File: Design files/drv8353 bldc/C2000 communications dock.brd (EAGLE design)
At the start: 160 x 100 mm, 3 parts, among them IC1 ADUM1311ARWZ, J3 SS-6488-NF-A431

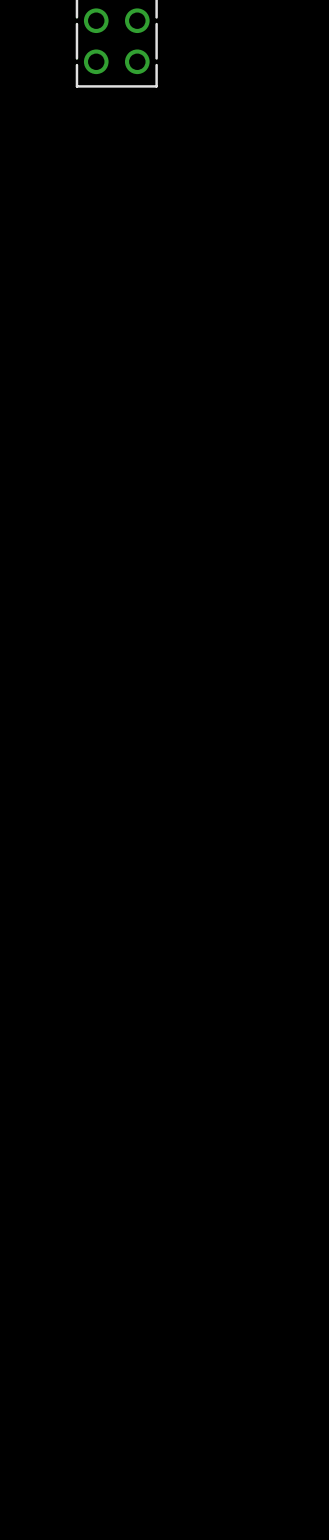
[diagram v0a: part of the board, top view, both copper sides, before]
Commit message: did some wiring and added led's
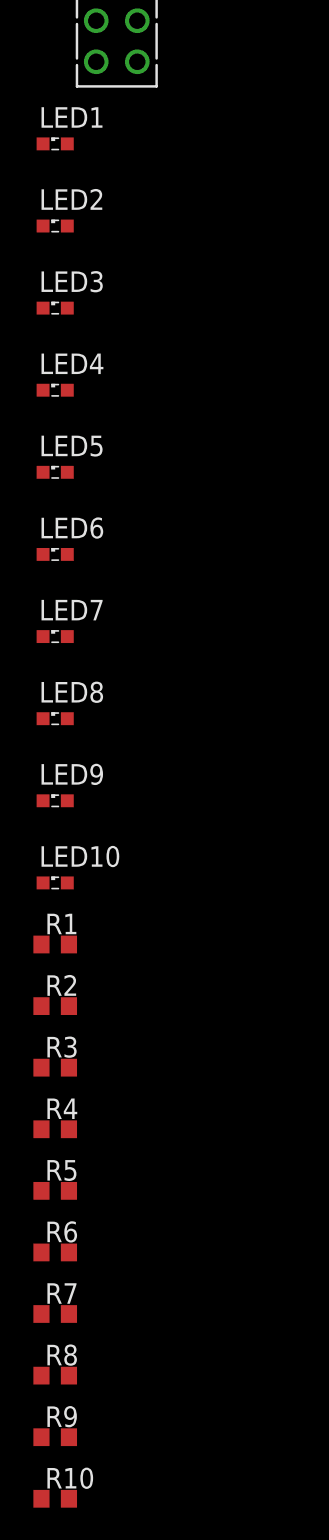
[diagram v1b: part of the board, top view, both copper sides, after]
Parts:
- added LED1, LED10, LED2, LED3, LED4, LED5, LED6, LED7, LED8, LED9: (no value), eagle-ltspice:LED_SML0603
- added R1, R10, R2, R3, R4, R5, R6, R7, R8, R9: 50, rcl:R0603
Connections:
- removed net 5V: U$1.21
- new net N$1: IC1.3, J3.3
- new net N$10: IC1.1, J3.1
- new net N$11: LED8.A, U$1.33
- new net N$12: LED9.A, U$1.32
- new net N$13: IC1.4, J3.4
- new net N$14: IC1.5, J3.5
- new net N$15: LED10.A, U$1.31
- new net N$16: IC1.2, IC1.7, IC1.8, J3.2
- new net N$17: LED1.C, R1.2
- new net N$18: LED2.C, R2.2
- new net N$19: LED3.C, R3.2
- new net N$2: LED1.A, U$1.40
- new net N$20: LED4.C, R4.2
- new net N$21: LED5.C, R5.2
- new net N$22: LED6.C, R6.2
- new net N$23: LED7.C, R7.2
- new net N$24: LED8.C, R8.2
- new net N$25: LED9.C, R9.2
- new net N$26: LED10.C, R10.2
- new net N$3: LED2.A, U$1.39
- new net N$4: LED3.A, U$1.38
- new net N$5: LED4.A, U$1.37
- new net N$6: LED5.A, U$1.36
- new net N$8: LED6.A, U$1.35
- new net N$9: LED7.A, U$1.34
- net 3.3V: now also IC1.16
- net CLK: now also IC1.13
- net GND: now also IC1.10, IC1.15, IC1.9, R1.1, R10.1, R2.1, R3.1, R4.1, R5.1, R6.1, R7.1, R8.1, R9.1, U$1.18
- net MISO: now also IC1.12
- net MOSI: now also IC1.14

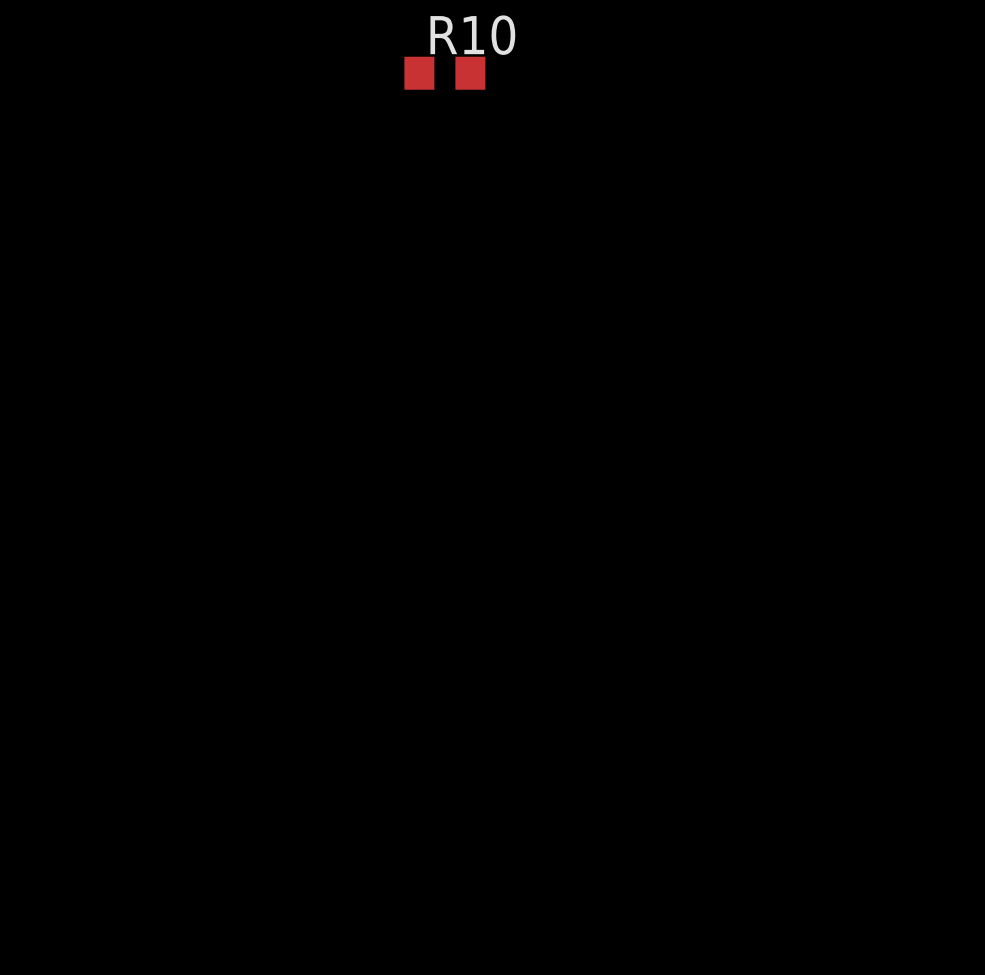
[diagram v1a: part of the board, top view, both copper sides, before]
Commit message: added pot, and headers for spi , i2c, analog pins, and the input spi signal
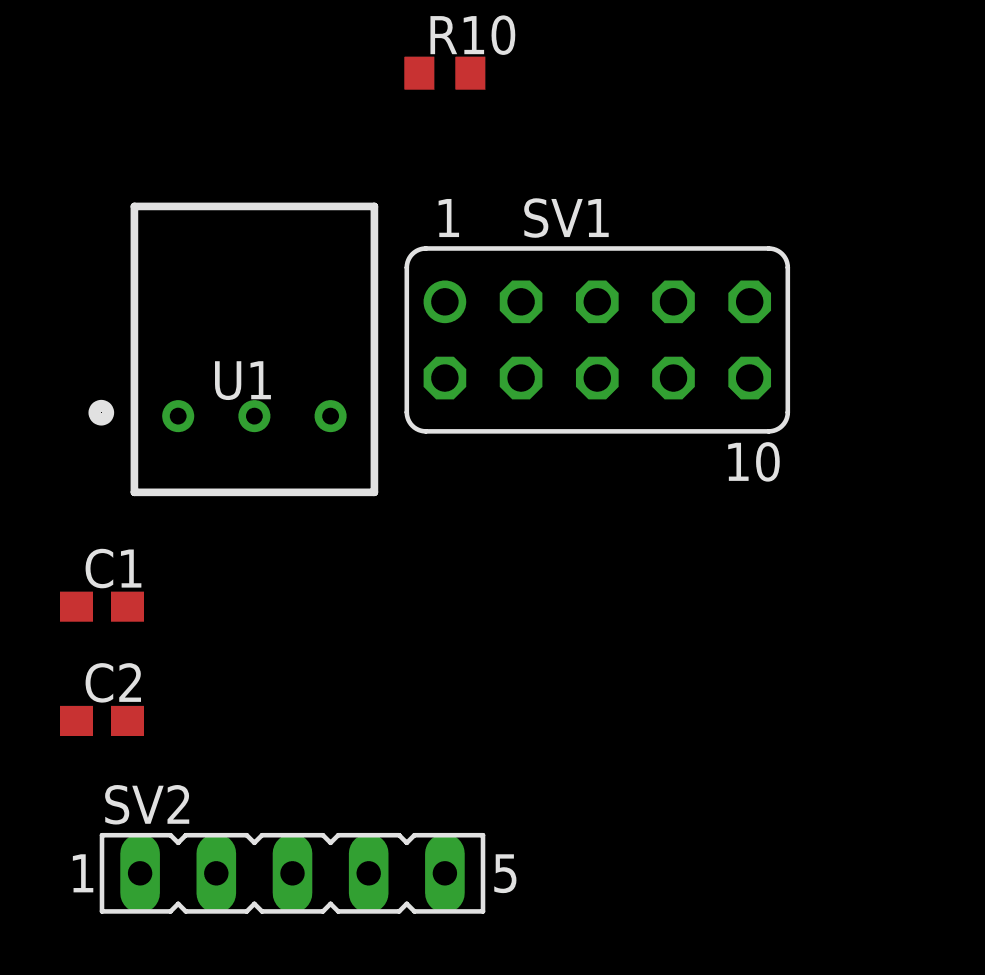
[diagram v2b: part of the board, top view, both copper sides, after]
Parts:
- added C1, C2: (no value), rcl:C0603
- added SV1: (no value), con-lsta:FE05-2
- added SV2: (no value), con-lsta:FE05-1
- added U1: 3352T-1-203LF, SamacSys_Parts:3352T-1-203LF
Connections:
- new net 5V: SV1.9, U$1.21
- new net AI1: SV1.8, U$1.23
- new net AI2: SV1.6, U$1.24
- new net POT: U$1.25, U1.2
- new net SCL: SV1.2, U$1.9
- new net SDA: SV1.4, U$1.10
- net 3.3V: now also C2.1, SV1.7, U1.3
- net CLK: now also SV1.5
- net GND: now also C2.2, SV1.10, U1.1; no longer U$1.18
- net MISO: now also SV1.1
- net MOSI: now also SV1.3
- net N$1: now also SV2.3
- net N$10: now also C1.1, SV2.1
- net N$13: now also SV2.4
- net N$14: now also SV2.5
- net N$16: now also C1.2, SV2.2

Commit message: reordered header and did a tenative layout
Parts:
- moved SV2 223.0 mm to (27.9, 40.6), turned to 180 degrees
- moved C1 213.3 mm to (29.3, 37.5), turned to 180 degrees
- moved C2 203.6 mm to (29.5, 23.5), turned to 180 degrees
- moved SV1 174.8 mm to (30.5, 10.7), turned to 270 degrees
- moved U1 174.0 mm to (17.8, 7.62), turned to 180 degrees
- moved R10 165.6 mm to (40.6, 5.08)
- moved R9 164.4 mm to (40.6, 7.62)
- moved R8 163.2 mm to (40.6, 10.2)
- moved R7 162.0 mm to (40.6, 12.7)
- moved R6 160.8 mm to (40.6, 15.2)
- moved R5 159.7 mm to (40.6, 17.8)
- moved R4 158.5 mm to (40.6, 20.3)
- moved R3 157.3 mm to (40.6, 22.9)
- moved R2 156.1 mm to (40.6, 25.4)
- moved R1 154.9 mm to (40.6, 27.9)
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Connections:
- net N$1 renamed EMOSI
- net N$10 renamed EVD
- net N$13 renamed ECLK
- net N$14 renamed EMISO
- net N$16 renamed EGND
- net 3.3V: now also SV1.1; no longer SV1.7
- net 5V: now also SV1.2; no longer SV1.9
- net AI1: now also SV1.4; no longer SV1.8
- net CLK: now also SV1.8; no longer SV1.5
- net GND: now also SV1.7; no longer SV1.10
- net MISO: now also SV1.5; no longer SV1.1
- net POT: now also U$1.28; no longer U$1.25
- net SCL: now also SV1.10; no longer SV1.2
- net SDA: now also SV1.9; no longer SV1.4
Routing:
- net 3.3V: track 0.00 -> 70.1 mm
- net CLK: track 0.00 -> 41.0 mm, vias 0 -> 2
- net MISO: track 0.00 -> 37.9 mm
- net GND: track 0.00 -> 37.5 mm, vias 0 -> 20
- net MOSI: track 0.00 -> 37.4 mm, vias 0 -> 2
- net SDA: track 0.00 -> 28.1 mm
- net 5V: track 0.00 -> 26.6 mm
- net EVD: track 0.00 -> 26.1 mm
- net AI2: track 0.00 -> 25.6 mm
- net AI1: track 0.00 -> 25.6 mm
- net SCL: track 0.00 -> 25.4 mm
- net EGND: track 0.00 -> 20.6 mm, vias 0 -> 2
- net EMOSI: track 0.00 -> 20.3 mm
- net EMISO: track 0.00 -> 13.8 mm
- net ECLK: track 0.00 -> 13.3 mm
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- added copper zone on layer 16, net EGND
- added copper zone on layer 16, net GND
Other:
- board size 160 x 100 mm -> 55.9 x 53 mm

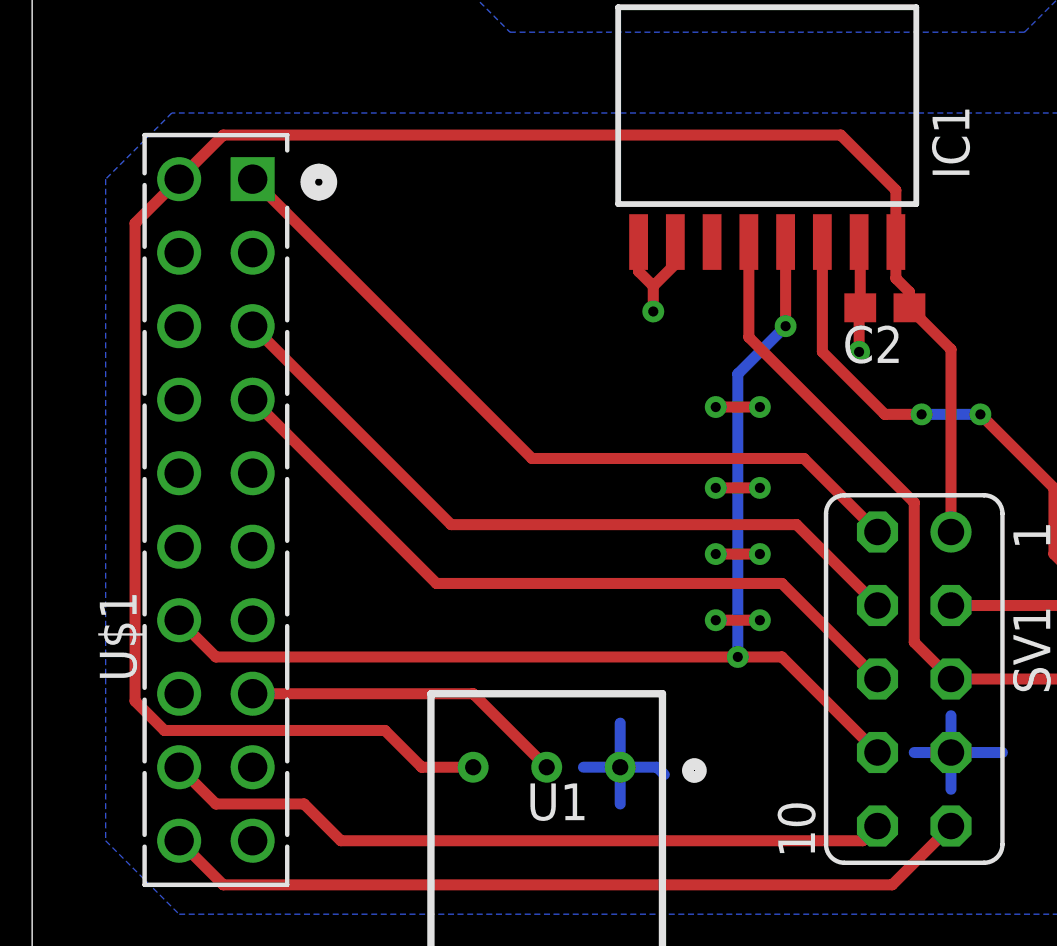
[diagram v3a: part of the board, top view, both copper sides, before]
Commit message: moved analog signals top adc-b pins
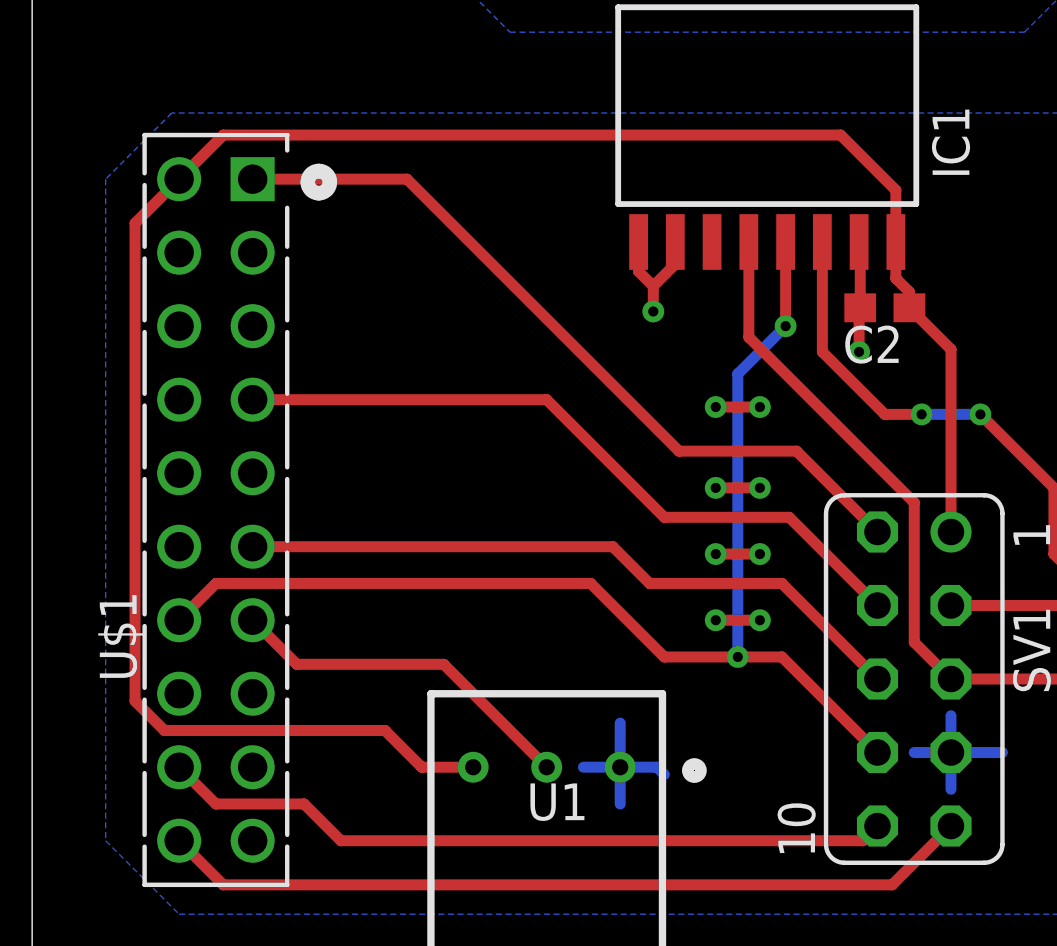
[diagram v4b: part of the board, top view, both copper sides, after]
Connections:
- net AI1: now also U$1.24; no longer U$1.23
- net AI2: now also U$1.26; no longer U$1.24
- net POT: now also U$1.27; no longer U$1.28
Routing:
- net AI2: track 25.6 -> 23.5 mm
- net AI1: track 25.6 -> 24.5 mm
- net POT: track 11.2 -> 12.3 mm
- net CLK: track 41.0 -> 42.1 mm
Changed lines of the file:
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@@
 <contactref element="SV1" pad="8"/>
 <wire x1="29.21" y1="8.128" x2="25.908" y2="11.43" width="0.381" layer="1"/>
-<wire x1="6.35" y1="11.43" x2="5.08" y2="12.7" width="0.381" layer="1"/>
 <wire x1="25.908" y1="11.43" x2="24.384" y2="11.43" width="0.381" layer="1"/>
-<wire x1="24.384" y1="11.43" x2="6.35" y2="11.43" width="0.381" layer="1"/>
 <via x="24.384" y="11.43" extent="1-16" drill="0.35"/>
 <via x="26.035" y="22.86" extent="1-16" drill="0.35"/>
@@
 <wire x1="24.384" y1="21.209" x2="26.035" y2="22.86" width="0.381" layer="16"/>
 <wire x1="26.035" y1="22.86" x2="26.035" y2="25.768" width="0.381" layer="1"/>
+<wire x1="24.384" y1="11.43" x2="21.844" y2="11.43" width="0.381" layer="1"/>
+<wire x1="19.304" y1="13.97" x2="6.35" y2="13.97" width="0.381" layer="1"/>
+<wire x1="6.35" y1="13.97" x2="5.08" y2="12.7" width="0.381" layer="1"/>
+<wire x1="21.844" y1="11.43" x2="19.304" y2="13.97" width="0.381" layer="1"/>
 </signal>
 <signal name="EVD">
@@
 <contactref element="U$1" pad="21"/>
 <contactref element="SV1" pad="2"/>
-<wire x1="29.21" y1="15.748" x2="26.67" y2="18.288" width="0.381" layer="1"/>
-<wire x1="17.272" y1="18.288" x2="7.62" y2="27.94" width="0.381" layer="1"/>
-<wire x1="26.67" y1="18.288" x2="17.272" y2="18.288" width="0.381" layer="1"/>
+<wire x1="22.352" y1="18.542" x2="12.954" y2="27.94" width="0.381" layer="1"/>
+<wire x1="12.954" y1="27.94" x2="7.62" y2="27.94" width="0.381" layer="1"/>
+<wire x1="29.21" y1="15.748" x2="26.416" y2="18.542" width="0.381" layer="1"/>
+<wire x1="26.416" y1="18.542" x2="22.352" y2="18.542" width="0.381" layer="1"/>
 </signal>
 <signal name="AI1">
-<contactref element="U$1" pad="23"/>
 <contactref element="SV1" pad="4"/>
-<wire x1="29.21" y1="13.208" x2="26.416" y2="16.002" width="0.381" layer="1"/>
-<wire x1="14.478" y1="16.002" x2="7.62" y2="22.86" width="0.381" layer="1"/>
-<wire x1="26.416" y1="16.002" x2="14.478" y2="16.002" width="0.381" layer="1"/>
+<contactref element="U$1" pad="24"/>
+<wire x1="21.844" y1="16.256" x2="17.78" y2="20.32" width="0.381" layer="1"/>
+<wire x1="17.78" y1="20.32" x2="7.62" y2="20.32" width="0.381" layer="1"/>
+<wire x1="29.21" y1="13.208" x2="26.162" y2="16.256" width="0.381" layer="1"/>
+<wire x1="26.162" y1="16.256" x2="21.844" y2="16.256" width="0.381" layer="1"/>
 </signal>
 <signal name="AI2">
-<contactref element="U$1" pad="24"/>
 <contactref element="SV1" pad="6"/>
+<contactref element="U$1" pad="26"/>
+<wire x1="21.336" y1="13.97" x2="20.066" y2="15.24" width="0.381" layer="1"/>
+<wire x1="20.066" y1="15.24" x2="7.62" y2="15.24" width="0.381" layer="1"/>
 <wire x1="29.21" y1="10.668" x2="25.908" y2="13.97" width="0.381" layer="1"/>
-<wire x1="13.97" y1="13.97" x2="7.62" y2="20.32" width="0.381" layer="1"/>
-<wire x1="25.908" y1="13.97" x2="13.97" y2="13.97" width="0.381" layer="1"/>
+<wire x1="25.908" y1="13.97" x2="21.336" y2="13.97" width="0.381" layer="1"/>
 </signal>
 <signal name="POT">
 <contactref element="U1" pad="2"/>
-<contactref element="U$1" pad="28"/>
-<wire x1="7.62" y1="10.16" x2="15.24" y2="10.16" width="0.381" layer="1"/>
-<wire x1="15.24" y1="10.16" x2="17.78" y2="7.62" width="0.381" layer="1"/>
+<contactref element="U$1" pad="27"/>
+<wire x1="9.144" y1="11.176" x2="7.62" y2="12.7" width="0.381" layer="1"/>
+<wire x1="17.78" y1="7.62" x2="14.224" y2="11.176" width="0.381" layer="1"/>
+<wire x1="14.224" y1="11.176" x2="9.144" y2="11.176" width="0.381" layer="1"/>
 </signal>
 </signals>
